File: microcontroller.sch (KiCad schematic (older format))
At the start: 62 parts, among them SW0 SW_Push, SW1 SW_Push, SW2 SW_Push, SW3 SW_Push, SW4 SW_Push, SW5 SW_Push

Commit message: FPGA cleanup
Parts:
- gave numbers to parts that had none: 6
- renumbered C_avdd to C_avdd1, C_dec to C_dec1, C_iovdd to C_iovdd1, C_reset to C_reset1, C_vdd to C_vdd1, R_disp to R_disp1, R_reset to R_reset1
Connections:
- net +3V3: now also J4.2, J4.3, J4.4, J4.5; no longer J4.3, J4.4, J4.5, J4.6
- net GND: now also J4.1; no longer J4.2
- net at U7.28 (PD0): now also J4.8; no longer J4.9
- net at U7.30 (PD2): now also J4.9; no longer J4.10
- net at U7.31 (PD3): now also J4.7; no longer J4.8
- net at J6.14: now also J4.6; no longer J4.7
- no-connect marks 11 -> 12
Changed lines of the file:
@@
 P 4450 2250
 AR Path="/5D7F7450" Ref="U?"  Part="1"
-AR Path="/5D7D441F/5D7F7450" Ref="U?"  Part="1"
-F 0 "U?" H 5550 2650 60  0000 C CNN
+AR Path="/5D7D441F/5D7F7450" Ref="U7"  Part="1"
+F 0 "U7" H 5550 2650 60  0000 C CNN
 F 1 "EFM32GG942F1024" H 5550 2550 60  0000 C CNN
 F 2 "QFP64_10X10" H 5550 2490 60  0001 C CNN
@@
 P 9950 3400
 AR Path="/5D7F9345" Ref="J?"  Part="1"
-AR Path="/5D7D441F/5D7F9345" Ref="J?"  Part="1"
-F 0 "J?" H 9750 4250 50  0000 R CNN
+AR Path="/5D7D441F/5D7F9345" Ref="J5"  Part="1"
+F 0 "J5" H 9750 4250 50  0000 R CNN
 F 1 "Conn_ARM_JTAG_SWD_20" H 9750 4150 50  0000 R BNN
 F 2 "" H 10400 2350 50  0001 L TNN
@@
 $EndComp
 $Comp
-L Effect-Box-rescue:C-dmpro-rescue C_dec
+L Effect-Box-rescue:C-dmpro-rescue C_dec1
 U 1 1 5D7F8CED
 P 7800 4350
-F 0 "C_dec" H 7825 4450 50  0000 L CNN
+F 0 "C_dec1" H 7825 4450 50  0000 L CNN
 F 1 "1 µF" H 7825 4250 50  0000 L CNN
 F 2 "" H 7838 4200 50  0001 C CNN
@@
 $EndComp
 $Comp
-L Device:C C_vdd
+L Device:C C_vdd1
 U 1 1 5D8125F5
 P 8500 4900
-F 0 "C_vdd" H 8615 4946 50  0000 L CNN
+F 0 "C_vdd1" H 8615 4946 50  0000 L CNN
 F 1 "10 µF" H 8615 4855 50  0000 L CNN
 F 2 "" H 8538 4750 50  0001 C CNN
@@
 Connection ~ 7800 3050
 $Comp
-L Device:C C_iovdd
+L Device:C C_iovdd1
 U 1 1 5D820429
 P 3400 1550
-F 0 "C_iovdd" H 3515 1596 50  0000 L CNN
+F 0 "C_iovdd1" H 3515 1596 50  0000 L CNN
 F 1 "10 µF" H 3515 1505 50  0000 L CNN
 F 2 "" H 3438 1400 50  0001 C CNN
@@
 Connection ~ 3950 4850
 $Comp
-L Device:C C_avdd
+L Device:C C_avdd1
 U 1 1 5D839716
 P 4400 6500
-F 0 "C_avdd" H 4515 6546 50  0000 L CNN
+F 0 "C_avdd1" H 4515 6546 50  0000 L CNN
 F 1 "10 µF" H 4515 6455 50  0000 L CNN
 F 2 "" H 4438 6350 50  0001 C CNN
@@
 	4400 6350 3800 6350
 $Comp
-L LCD:FH12A-10S-0.5SH55 J?
-U 2 1 5D86B092
+L LCD:FH12A-10S-0.5SH55 J4
+U 1 1 5D86B092
 P 4000 9050
-F 0 "J?" V 3450 9200 60  0000 L CNN
+F 0 "J4" V 3450 9200 60  0000 L CNN
 F 1 " " V 3800 8600 60  0000 L CNN
 F 2 "CONN10_1X10_DRC_FFC" H 4000 8990 60  0001 C CNN
 F 3 "" H 4000 9050 60  0000 C CNN
-	2    4000 9050
+	1    4000 9050
 	0    1    -1   0
 $EndComp
 $Comp
-L LCD:FH12A-10S-0.5SH55 J?
-U 3 1 5D873ACF
+L LCD:FH12A-10S-0.5SH55 J4
+U 2 1 5D873ACF
 P 4350 9050
-F 0 "J?" V 4100 9200 60  0000 C CNN
+F 0 "J4" V 4100 9200 60  0000 C CNN
 F 1 " " V 4550 9050 60  0000 C CNN
 F 2 "CONN10_1X10_DRC_FFC" H 4350 8990 60  0001 C CNN
 F 3 "" H 4350 9050 60  0000 C CNN
-	3    4350 9050
+	2    4350 9050
 	0    1    -1   0
 $EndComp
 $Comp
-L LCD:FH12A-10S-0.5SH55 J?
-U 4 1 5D88452F
+L LCD:FH12A-10S-0.5SH55 J4
+U 3 1 5D88452F
 P 4700 9050
-F 0 "J?" V 4442 9148 60  0000 L CNN
+F 0 "J4" V 4442 9148 60  0000 L CNN
 F 1 " " V 4548 9148 60  0000 L CNN
 F 2 "CONN10_1X10_DRC_FFC" H 4700 8990 60  0001 C CNN
 F 3 "" H 4700 9050 60  0000 C CNN
-	4    4700 9050
+	3    4700 9050
 	0    1    -1   0
 $EndComp
 $Comp
-L LCD:FH12A-10S-0.5SH55 J?
-U 5 1 5D88BAB2
+L LCD:FH12A-10S-0.5SH55 J4
+U 4 1 5D88BAB2
 P 5050 9050
-F 0 "J?" V 4792 9148 60  0000 L CNN
+F 0 "J4" V 4792 9148 60  0000 L CNN
 F 1 " " V 4898 9148 60  0000 L CNN
 F 2 "CONN10_1X10_DRC_FFC" H 5050 8990 60  0001 C CNN
 F 3 "" H 5050 9050 60  0000 C CNN
-	5    5050 9050
+	4    5050 9050
 	0    1    -1   0
 $EndComp
 $Comp
-L LCD:FH12A-10S-0.5SH55 J?
-U 6 1 5D891720
+L LCD:FH12A-10S-0.5SH55 J4
+U 5 1 5D891720
 P 5400 9050
-F 0 "J?" V 5142 9148 60  0000 L CNN
+F 0 "J4" V 5142 9148 60  0000 L CNN
 F 1 " " V 5248 9148 60  0000 L CNN
 F 2 "CONN10_1X10_DRC_FFC" H 5400 8990 60  0001 C CNN
 F 3 "" H 5400 9050 60  0000 C CNN
-	6    5400 9050
+	5    5400 9050
 	0    1    -1   0
 $EndComp
 $Comp
-L LCD:FH12A-10S-0.5SH55 J?
-U 7 1 5D89776E
+L LCD:FH12A-10S-0.5SH55 J4
+U 6 1 5D89776E
 P 5750 9050
-F 0 "J?" V 5492 9148 60  0000 L CNN
+F 0 "J4" V 5492 9148 60  0000 L CNN
 F 1 " " V 5598 9148 60  0000 L CNN
 F 2 "CONN10_1X10_DRC_FFC" H 5750 8990 60  0001 C CNN
 F 3 "" H 5750 9050 60  0000 C CNN
-	7    5750 9050
+	6    5750 9050
 	0    1    -1   0
 $EndComp
 $Comp
-L LCD:FH12A-10S-0.5SH55 J?
-U 8 1 5D89D729
+L LCD:FH12A-10S-0.5SH55 J4
+U 7 1 5D89D729
 P 6100 9050
-F 0 "J?" V 5842 9147 60  0000 L CNN
+F 0 "J4" V 5842 9147 60  0000 L CNN
 F 1 " " V 5948 9147 60  0000 L CNN
 F 2 "CONN10_1X10_DRC_FFC" H 6100 8990 60  0001 C CNN
 F 3 "" H 6100 9050 60  0000 C CNN
-	8    6100 9050
+	7    6100 9050
 	0    1    -1   0
 $EndComp
 $Comp
-L LCD:FH12A-10S-0.5SH55 J?
-U 9 1 5D8A2C47
+L LCD:FH12A-10S-0.5SH55 J4
+U 8 1 5D8A2C47
 P 6450 9050
-F 0 "J?" V 6192 9147 60  0000 L CNN
+F 0 "J4" V 6192 9147 60  0000 L CNN
 F 1 " " V 6298 9147 60  0000 L CNN
 F 2 "CONN10_1X10_DRC_FFC" H 6450 8990 60  0001 C CNN
 F 3 "" H 6450 9050 60  0000 C CNN
-	9    6450 9050
+	8    6450 9050
 	0    1    -1   0
 $EndComp
 $Comp
-L LCD:FH12A-10S-0.5SH55 J?
-U 10 1 5D8AB529
+L LCD:FH12A-10S-0.5SH55 J4
+U 9 1 5D8AB529
 P 6800 9050
-F 0 "J?" V 6513 9148 60  0000 L CNN
+F 0 "J4" V 6513 9148 60  0000 L CNN
 F 1 " " V 6619 9148 60  0000 L CNN
 F 2 "CONN10_1X10_DRC_FFC" H 6800 8990 60  0001 C CNN
 F 3 "" H 6800 9050 60  0000 C CNN
-	10   6800 9050
+	9    6800 9050
 	0    1    -1   0
 $EndComp
 $Comp
-L LCD:FH12A-10S-0.5SH55 J?
-U 11 1 5D8B1A3C
+L LCD:FH12A-10S-0.5SH55 J4
+U 10 1 5D8B1A3C
 P 7150 9050
-F 0 "J?" V 6863 9148 60  0000 L CNN
+F 0 "J4" V 6863 9148 60  0000 L CNN
 F 1 " " V 6969 9148 60  0000 L CNN
 F 2 "CONN10_1X10_DRC_FFC" H 7150 8990 60  0001 C CNN
 F 3 "" H 7150 9050 60  0000 C CNN
-	11   7150 9050
+	10   7150 9050
 	0    1    -1   0
 $EndComp
 $Comp
-L LCD:FH12A-10S-0.5SH55 J?
-U 12 1 5D8B82A9
+L LCD:FH12A-10S-0.5SH55 J4
+U 11 1 5D8B82A9
 P 7500 9050
-F 0 "J?" V 7213 9147 60  0000 L CNN
+F 0 "J4" V 7213 9147 60  0000 L CNN
 F 1 " " V 7319 9147 60  0000 L CNN
 F 2 "CONN10_1X10_DRC_FFC" H 7500 8990 60  0001 C CNN
 F 3 "" H 7500 9050 60  0000 C CNN
-	12   7500 9050
+	11   7500 9050
 	0    1    -1   0
 $EndComp
@@
 $EndComp
 $Comp
-L LCD:FH12A-10S-0.5SH55 J?
+L LCD:FH12A-10S-0.5SH55 J3
 U 1 1 5D85CD0B
 P 3650 9050
-F 0 "J?" V 3100 9250 60  0000 C CNN
+F 0 "J3" V 3100 9250 60  0000 C CNN
 F 1 "FH12A-10S-0.5SH55" V 3050 10800 60  0000 C CNN
 F 2 "CONN10_1X10_DRC_FFC" H 3650 8990 60  0001 C CNN
@@
 Connection ~ 5400 8950
 $Comp
-L Device:R R_disp
+L Device:R R_disp1
 U 1 1 5D8D60C6
 P 3650 8600
-F 0 "R_disp" V 3443 8600 50  0000 C CNN
+F 0 "R_disp1" V 3443 8600 50  0000 C CNN
 F 1 "10 MΩ" V 3534 8600 50  0000 C CNN
 F 2 "" V 3580 8600 50  0001 C CNN
@@
 	600  1300 600  1100
 $Comp
-L Device:R R_reset
+L Device:R R_reset1
 U 1 1 5D97B808
 P 950 3450
-F 0 "R_reset" V 743 3450 50  0000 C CNN
+F 0 "R_reset1" V 743 3450 50  0000 C CNN
 F 1 "100 Ω" V 834 3450 50  0000 C CNN
 F 2 "" V 880 3450 50  0001 C CNN
@@
 	800  3450 700  3450
 $Comp
-L Device:C C_reset
+L Device:C C_reset1
 U 1 1 5D98246A
 P 1700 3600
-F 0 "C_reset" H 1300 3550 50  0000 L CNN
+F 0 "C_reset1" H 1300 3550 50  0000 L CNN
 F 1 "100 nF" H 1300 3450 50  0000 L CNN
 F 2 "" H 1738 3450 50  0001 C CNN
@@
 Connection ~ -2100 1200
 $Comp
-L Switch:SW_Push SW?
+L Switch:SW_Push SW6
 U 1 1 5D97A033
 P 1300 3450
-F 0 "SW?" H 1300 3735 50  0000 C CNN
+F 0 "SW6" H 1300 3735 50  0000 C CNN
 F 1 "SW_Push" H 1300 3644 50  0000 C CNN
 F 2 "" H 1300 3650 50  0001 C CNN
@@
 	4150 3050 4450 3050
 $Comp
-L pin_header:26642801RP2 J?
+L pin_header:26642801RP2 J6
 U 1 1 5DFD015B
 P 12150 4850
-F 0 "J?" H 13150 5237 60  0000 C CNN
+F 0 "J6" H 13150 5237 60  0000 C CNN
 F 1 "26642801RP2" H 13150 5131 60  0000 C CNN
 F 2 "CON28_2X14_HDR_2664" H 13150 5090 60  0001 C CNN
@@
 NoConn ~ 6650 5350
 NoConn ~ 4450 5350
+NoConn ~ 4450 4050
 $EndSCHEMATC

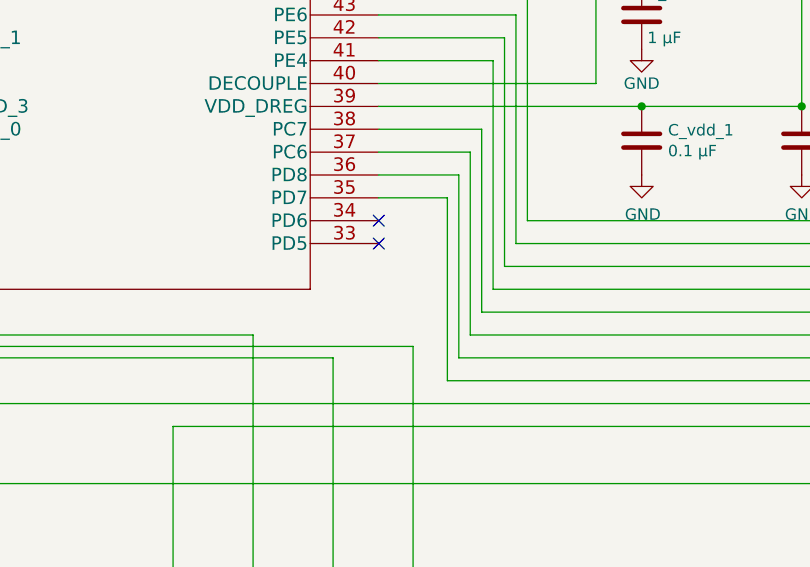
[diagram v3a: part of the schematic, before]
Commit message: Minor FPGA and MCU fixes
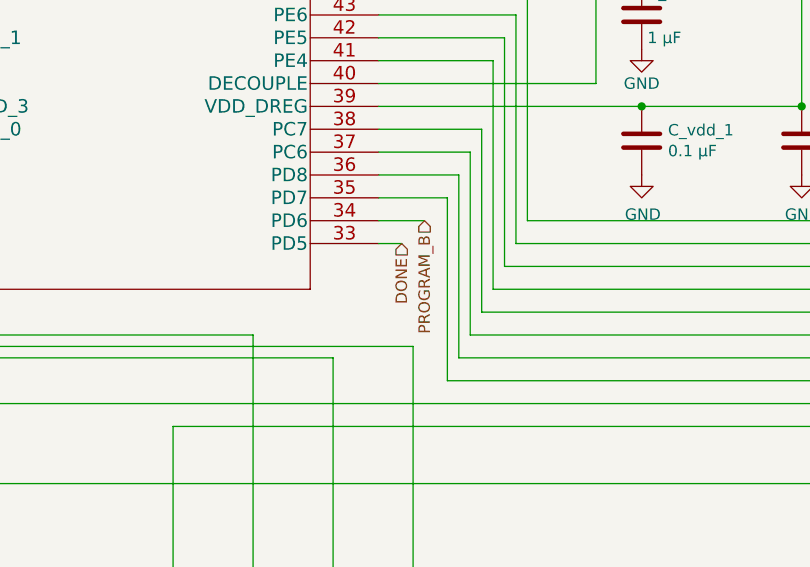
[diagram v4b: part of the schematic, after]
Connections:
- net DONE: now reaches U7.33 (PD5)
- net PROGRAM_B: now reaches U7.34 (PD6)
- no-connect marks 12 -> 10
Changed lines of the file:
@@
 Wire Wire Line
 	14150 6400 14150 6150
-NoConn ~ 6650 5250
-NoConn ~ 6650 5350
 NoConn ~ 4450 5350
 NoConn ~ 4450 4050
+Text HLabel 6850 5250 3    50   Input ~ 0
+PROGRAM_B
+Text HLabel 6750 5350 3    50   Input ~ 0
+DONE
+Wire Wire Line
+	6750 5350 6650 5350
+Wire Wire Line
+	6650 5250 6850 5250
 $EndSCHEMATC

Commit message: Add various footprints
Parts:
- C_avdd1, C_avdd_0, C_avdd_1, C_btn_0, C_btn_1, C_btn_2, C_btn_3, C_btn_4, C_btn_5, C_crystal_1, C_crystal_2, C_dec1, C_disp_1, C_disp_2, C_iovdd1, C_iovdd_0, C_iovdd_3, C_iovdd_5, C_reset1, C_vdd1, C_vdd_1: footprint (none) -> Capacitor_SMD:C_1206_3216Metric_Pad1.42x1.75mm_HandSolder
- R_LED_1, R_LED_2, R_btn_0, R_btn_1, R_btn_2, R_btn_3, R_btn_4, R_btn_5, R_btn_up_0, R_btn_up_1, R_btn_up_2, R_btn_up_3, R_btn_up_4, R_btn_up_5, R_disp1, R_reset1: footprint (none) -> Resistor_SMD:R_1206_3216Metric_Pad1.42x1.75mm_HandSolder
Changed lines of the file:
@@
 F 0 "C_crystal_2" H 2625 6650 50  0000 L CNN
 F 1 "12 pF" H 2625 6450 50  0000 L CNN
-F 2 "" H 2638 6400 50  0001 C CNN
+F 2 "Capacitor_SMD:C_1206_3216Metric_Pad1.42x1.75mm_HandSolder" H 2638 6400 50  0001 C CNN
 F 3 "" H 2600 6550 50  0001 C CNN
 	1    2600 6550
@@
 F 0 "C_crystal_1" H 1625 6650 50  0000 L CNN
 F 1 "12 pF" H 1625 6450 50  0000 L CNN
-F 2 "" H 1638 6400 50  0001 C CNN
+F 2 "Capacitor_SMD:C_1206_3216Metric_Pad1.42x1.75mm_HandSolder" H 1638 6400 50  0001 C CNN
 F 3 "" H 1600 6550 50  0001 C CNN
 	1    1600 6550
@@
 F 0 "C_dec1" H 7825 4450 50  0000 L CNN
 F 1 "1 µF" H 7825 4250 50  0000 L CNN
-F 2 "" H 7838 4200 50  0001 C CNN
+F 2 "Capacitor_SMD:C_1206_3216Metric_Pad1.42x1.75mm_HandSolder" H 7838 4200 50  0001 C CNN
 F 3 "" H 7800 4350 50  0001 C CNN
 	1    7800 4350
@@
 F 0 "C_vdd_1" H 7915 4946 50  0000 L CNN
 F 1 "0.1 µF" H 7915 4855 50  0000 L CNN
-F 2 "" H 7838 4750 50  0001 C CNN
+F 2 "Capacitor_SMD:C_1206_3216Metric_Pad1.42x1.75mm_HandSolder" H 7838 4750 50  0001 C CNN
 F 3 "~" H 7800 4900 50  0001 C CNN
 	1    7800 4900
@@
 F 0 "C_vdd1" H 8615 4946 50  0000 L CNN
 F 1 "10 µF" H 8615 4855 50  0000 L CNN
-F 2 "" H 8538 4750 50  0001 C CNN
+F 2 "Capacitor_SMD:C_1206_3216Metric_Pad1.42x1.75mm_HandSolder" H 8538 4750 50  0001 C CNN
 F 3 "~" H 8500 4900 50  0001 C CNN
 	1    8500 4900
@@
 F 0 "C_iovdd_3" H 3515 4946 50  0000 L CNN
 F 1 "0.1 µF" H 3515 4855 50  0000 L CNN
-F 2 "" H 3438 4750 50  0001 C CNN
+F 2 "Capacitor_SMD:C_1206_3216Metric_Pad1.42x1.75mm_HandSolder" H 3438 4750 50  0001 C CNN
 F 3 "~" H 3400 4900 50  0001 C CNN
 	1    3400 4900
@@
 F 0 "C_iovdd_5" H 8315 3196 50  0000 L CNN
 F 1 "0.1 µF" H 8315 3105 50  0000 L CNN
-F 2 "" H 8238 3000 50  0001 C CNN
+F 2 "Capacitor_SMD:C_1206_3216Metric_Pad1.42x1.75mm_HandSolder" H 8238 3000 50  0001 C CNN
 F 3 "~" H 8200 3150 50  0001 C CNN
 	1    8200 3150
@@
 F 0 "C_iovdd1" H 3515 1596 50  0000 L CNN
 F 1 "10 µF" H 3515 1505 50  0000 L CNN
-F 2 "" H 3438 1400 50  0001 C CNN
+F 2 "Capacitor_SMD:C_1206_3216Metric_Pad1.42x1.75mm_HandSolder" H 3438 1400 50  0001 C CNN
 F 3 "~" H 3400 1550 50  0001 C CNN
 	1    3400 1550
@@
 F 0 "C_avdd_1" H 3915 6546 50  0000 L CNN
 F 1 "10 nF" H 3915 6455 50  0000 L CNN
-F 2 "" H 3838 6350 50  0001 C CNN
+F 2 "Capacitor_SMD:C_1206_3216Metric_Pad1.42x1.75mm_HandSolder" H 3838 6350 50  0001 C CNN
 F 3 "~" H 3800 6500 50  0001 C CNN
 	1    3800 6500
@@
 F 0 "C_avdd_0" H 3365 6546 50  0000 L CNN
 F 1 "10 nF" H 3365 6455 50  0000 L CNN
-F 2 "" H 3288 6350 50  0001 C CNN
+F 2 "Capacitor_SMD:C_1206_3216Metric_Pad1.42x1.75mm_HandSolder" H 3288 6350 50  0001 C CNN
 F 3 "~" H 3250 6500 50  0001 C CNN
 	1    3250 6500
@@
 F 0 "C_avdd1" H 4515 6546 50  0000 L CNN
 F 1 "10 µF" H 4515 6455 50  0000 L CNN
-F 2 "" H 4438 6350 50  0001 C CNN
+F 2 "Capacitor_SMD:C_1206_3216Metric_Pad1.42x1.75mm_HandSolder" H 4438 6350 50  0001 C CNN
 F 3 "~" H 4400 6500 50  0001 C CNN
 	1    4400 6500
@@
 F 0 "R_disp1" V 3443 8600 50  0000 C CNN
 F 1 "10 MΩ" V 3534 8600 50  0000 C CNN
-F 2 "" V 3580 8600 50  0001 C CNN
+F 2 "Resistor_SMD:R_1206_3216Metric_Pad1.42x1.75mm_HandSolder" V 3580 8600 50  0001 C CNN
 F 3 "~" H 3650 8600 50  0001 C CNN
 	1    3650 8600
@@
 F 0 "C_disp_1" H 3115 8796 50  0000 L CNN
 F 1 "100 nF" H 3115 8705 50  0000 L CNN
-F 2 "" H 3038 8600 50  0001 C CNN
+F 2 "Capacitor_SMD:C_1206_3216Metric_Pad1.42x1.75mm_HandSolder" H 3038 8600 50  0001 C CNN
 F 3 "~" H 3000 8750 50  0001 C CNN
 	1    3000 8750
@@
 F 0 "C_disp_2" H 2200 8800 50  0000 L CNN
 F 1 "100 nF" H 2250 8700 50  0000 L CNN
-F 2 "" H 2688 8600 50  0001 C CNN
+F 2 "Capacitor_SMD:C_1206_3216Metric_Pad1.42x1.75mm_HandSolder" H 2688 8600 50  0001 C CNN
 F 3 "~" H 2650 8750 50  0001 C CNN
 	1    2650 8750
@@
 F 0 "R_LED_1" H 2050 3800 50  0000 L CNN
 F 1 "82 Ω" H 2050 3700 50  0000 L CNN
-F 2 "" V 1930 3750 50  0001 C CNN
+F 2 "Resistor_SMD:R_1206_3216Metric_Pad1.42x1.75mm_HandSolder" V 1930 3750 50  0001 C CNN
 F 3 "~" H 2000 3750 50  0001 C CNN
 	1    2000 3750
@@
 F 0 "R_LED_2" H 2450 3800 50  0000 L CNN
 F 1 "82 Ω" H 2450 3700 50  0000 L CNN
-F 2 "" V 2330 3750 50  0001 C CNN
+F 2 "Resistor_SMD:R_1206_3216Metric_Pad1.42x1.75mm_HandSolder" V 2330 3750 50  0001 C CNN
 F 3 "~" H 2400 3750 50  0001 C CNN
 	1    2400 3750
@@
 F 0 "C_iovdd_0" H 3515 2096 50  0000 L CNN
 F 1 "0.1 µF" H 3515 2005 50  0000 L CNN
-F 2 "" H 3438 1900 50  0001 C CNN
+F 2 "Capacitor_SMD:C_1206_3216Metric_Pad1.42x1.75mm_HandSolder" H 3438 1900 50  0001 C CNN
 F 3 "~" H 3400 2050 50  0001 C CNN
 	1    3400 2050
@@
 F 0 "R_reset1" V 743 3450 50  0000 C CNN
 F 1 "100 Ω" V 834 3450 50  0000 C CNN
-F 2 "" V 880 3450 50  0001 C CNN
+F 2 "Resistor_SMD:R_1206_3216Metric_Pad1.42x1.75mm_HandSolder" V 880 3450 50  0001 C CNN
 F 3 "~" H 950 3450 50  0001 C CNN
 	1    950  3450
@@
 F 0 "C_reset1" H 1300 3550 50  0000 L CNN
 F 1 "100 nF" H 1300 3450 50  0000 L CNN
-F 2 "" H 1738 3450 50  0001 C CNN
+F 2 "Capacitor_SMD:C_1206_3216Metric_Pad1.42x1.75mm_HandSolder" H 1738 3450 50  0001 C CNN
 F 3 "~" H 1700 3600 50  0001 C CNN
 	1    1700 3600
@@
 F 0 "R_btn_0" H 2320 246 50  0000 L CNN
 F 1 "100 Ω" H 2320 155 50  0000 L CNN
-F 2 "" V 2180 200 50  0001 C CNN
+F 2 "Resistor_SMD:R_1206_3216Metric_Pad1.42x1.75mm_HandSolder" V 2180 200 50  0001 C CNN
 F 3 "~" H 2250 200 50  0001 C CNN
 	1    2250 200
@@
 F 0 "R_btn_2" H 1220 246 50  0000 L CNN
 F 1 "100 Ω" H 1220 155 50  0000 L CNN
-F 2 "" V 1080 200 50  0001 C CNN
+F 2 "Resistor_SMD:R_1206_3216Metric_Pad1.42x1.75mm_HandSolder" V 1080 200 50  0001 C CNN
 F 3 "~" H 1150 200 50  0001 C CNN
 	1    1150 200
@@
 F 0 "R_btn_3" H 670 246 50  0000 L CNN
 F 1 "100 Ω" H 670 155 50  0000 L CNN
-F 2 "" V 530 200 50  0001 C CNN
+F 2 "Resistor_SMD:R_1206_3216Metric_Pad1.42x1.75mm_HandSolder" V 530 200 50  0001 C CNN
 F 3 "~" H 600 200 50  0001 C CNN
 	1    600  200
@@
 F 0 "R_btn_4" H 1220 2146 50  0000 L CNN
 F 1 "100 Ω" H 1220 2055 50  0000 L CNN
-F 2 "" V 1080 2100 50  0001 C CNN
+F 2 "Resistor_SMD:R_1206_3216Metric_Pad1.42x1.75mm_HandSolder" V 1080 2100 50  0001 C CNN
 F 3 "~" H 1150 2100 50  0001 C CNN
 	1    1150 2100
@@
 F 0 "R_btn_5" H 670 2146 50  0000 L CNN
 F 1 "100 Ω" H 670 2055 50  0000 L CNN
-F 2 "" V 530 2100 50  0001 C CNN
+F 2 "Resistor_SMD:R_1206_3216Metric_Pad1.42x1.75mm_HandSolder" V 530 2100 50  0001 C CNN
 F 3 "~" H 600 2100 50  0001 C CNN
 	1    600  2100
@@
 F 0 "R_btn_1" H 1770 246 50  0000 L CNN
 F 1 "100 Ω" H 1770 155 50  0000 L CNN
-F 2 "" V 1630 200 50  0001 C CNN
+F 2 "Resistor_SMD:R_1206_3216Metric_Pad1.42x1.75mm_HandSolder" V 1630 200 50  0001 C CNN
 F 3 "~" H 1700 200 50  0001 C CNN
 	1    1700 200
@@
 F 0 "C_btn_5" H -3100 2300 50  0000 L CNN
 F 1 "1 nF" H -3085 2205 50  0000 L CNN
-F 2 "" H -3162 2100 50  0001 C CNN
+F 2 "Capacitor_SMD:C_1206_3216Metric_Pad1.42x1.75mm_HandSolder" H -3162 2100 50  0001 C CNN
 F 3 "~" H -3200 2250 50  0001 C CNN
 	1    -3200 2250
@@
 F 0 "C_btn_3" H -2000 2300 50  0000 L CNN
 F 1 "1 nF" H -2000 2200 50  0000 L CNN
-F 2 "" H -2062 2100 50  0001 C CNN
+F 2 "Capacitor_SMD:C_1206_3216Metric_Pad1.42x1.75mm_HandSolder" H -2062 2100 50  0001 C CNN
 F 3 "~" H -2100 2250 50  0001 C CNN
 	1    -2100 2250
@@
 F 0 "C_btn_2" H -1450 2300 50  0000 L CNN
 F 1 "1 nF" H -1450 2200 50  0000 L CNN
-F 2 "" H -1512 2100 50  0001 C CNN
+F 2 "Capacitor_SMD:C_1206_3216Metric_Pad1.42x1.75mm_HandSolder" H -1512 2100 50  0001 C CNN
 F 3 "~" H -1550 2250 50  0001 C CNN
 	1    -1550 2250
@@
 F 0 "C_btn_1" H -900 2300 50  0000 L CNN
 F 1 "1 nF" H -900 2200 50  0000 L CNN
-F 2 "" H -962 2100 50  0001 C CNN
+F 2 "Capacitor_SMD:C_1206_3216Metric_Pad1.42x1.75mm_HandSolder" H -962 2100 50  0001 C CNN
 F 3 "~" H -1000 2250 50  0001 C CNN
 	1    -1000 2250
@@
 F 0 "C_btn_0" H -350 2300 50  0000 L CNN
 F 1 "1 nF" H -350 2200 50  0000 L CNN
-F 2 "" H -412 2100 50  0001 C CNN
+F 2 "Capacitor_SMD:C_1206_3216Metric_Pad1.42x1.75mm_HandSolder" H -412 2100 50  0001 C CNN
 F 3 "~" H -450 2250 50  0001 C CNN
 	1    -450 2250
@@
 F 0 "R_btn_up_5" H -3130 1696 50  0000 L CNN
 F 1 "1 MΩ" H -3130 1605 50  0000 L CNN
-F 2 "" V -3270 1650 50  0001 C CNN
+F 2 "Resistor_SMD:R_1206_3216Metric_Pad1.42x1.75mm_HandSolder" V -3270 1650 50  0001 C CNN
 F 3 "~" H -3200 1650 50  0001 C CNN
 	1    -3200 1650
@@
 F 0 "R_btn_up_4" H -2580 1696 50  0000 L CNN
 F 1 "1 MΩ" H -2580 1605 50  0000 L CNN
-F 2 "" V -2720 1650 50  0001 C CNN
+F 2 "Resistor_SMD:R_1206_3216Metric_Pad1.42x1.75mm_HandSolder" V -2720 1650 50  0001 C CNN
 F 3 "~" H -2650 1650 50  0001 C CNN
 	1    -2650 1650
@@
 F 0 "R_btn_up_3" H -2030 1696 50  0000 L CNN
 F 1 "1 MΩ" H -2030 1605 50  0000 L CNN
-F 2 "" V -2170 1650 50  0001 C CNN
+F 2 "Resistor_SMD:R_1206_3216Metric_Pad1.42x1.75mm_HandSolder" V -2170 1650 50  0001 C CNN
 F 3 "~" H -2100 1650 50  0001 C CNN
 	1    -2100 1650
@@
 F 0 "R_btn_up_2" H -1480 1696 50  0000 L CNN
 F 1 "1 MΩ" H -1480 1605 50  0000 L CNN
-F 2 "" V -1620 1650 50  0001 C CNN
+F 2 "Resistor_SMD:R_1206_3216Metric_Pad1.42x1.75mm_HandSolder" V -1620 1650 50  0001 C CNN
 F 3 "~" H -1550 1650 50  0001 C CNN
 	1    -1550 1650
@@
 F 0 "R_btn_up_1" H -930 1696 50  0000 L CNN
 F 1 "1 MΩ" H -930 1605 50  0000 L CNN
-F 2 "" V -1070 1650 50  0001 C CNN
+F 2 "Resistor_SMD:R_1206_3216Metric_Pad1.42x1.75mm_HandSolder" V -1070 1650 50  0001 C CNN
 F 3 "~" H -1000 1650 50  0001 C CNN
 	1    -1000 1650
@@
 F 0 "R_btn_up_0" H -380 1696 50  0000 L CNN
 F 1 "1 MΩ" H -380 1605 50  0000 L CNN
-F 2 "" V -520 1650 50  0001 C CNN
+F 2 "Resistor_SMD:R_1206_3216Metric_Pad1.42x1.75mm_HandSolder" V -520 1650 50  0001 C CNN
 F 3 "~" H -450 1650 50  0001 C CNN
 	1    -450 1650
@@
 F 0 "C_btn_4" H -2550 2300 50  0000 L CNN
 F 1 "1 nF" H -2535 2205 50  0000 L CNN
-F 2 "" H -2612 2100 50  0001 C CNN
+F 2 "Capacitor_SMD:C_1206_3216Metric_Pad1.42x1.75mm_HandSolder" H -2612 2100 50  0001 C CNN
 F 3 "~" H -2650 2250 50  0001 C CNN
 	1    -2650 2250
